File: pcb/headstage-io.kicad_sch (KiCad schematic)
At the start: 5 parts, among them J2 BTE-040-03-L-D-A, J3 BTE-040-03-L-D-A

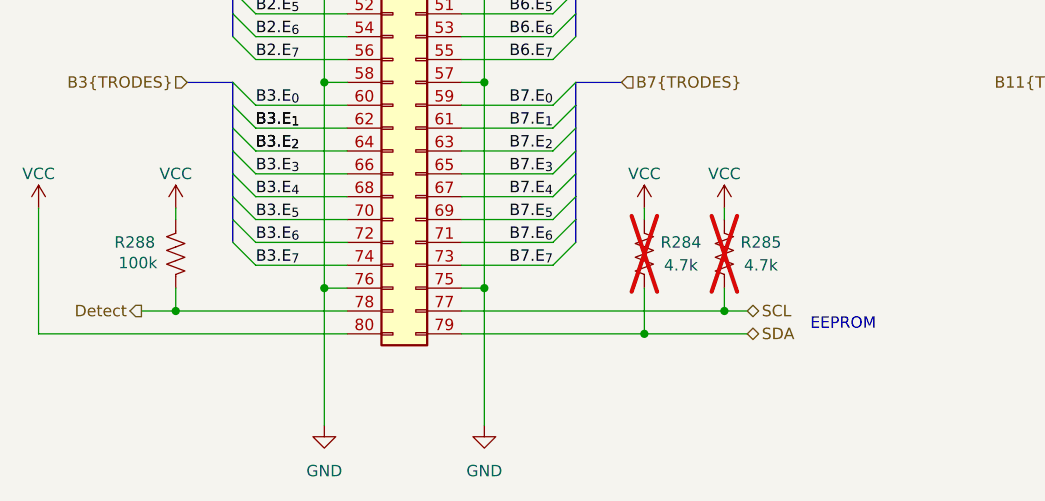
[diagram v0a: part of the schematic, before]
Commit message: Fix electrode coupling
- AC coupling follows attentuation to prevent high-pass filtering
- Remove redundant i2c pullups (can be enabled in MCU if really needed)
- Replace detect line with WP/Detect so that this device can be used to
  program module EEPROM by pulling the line down
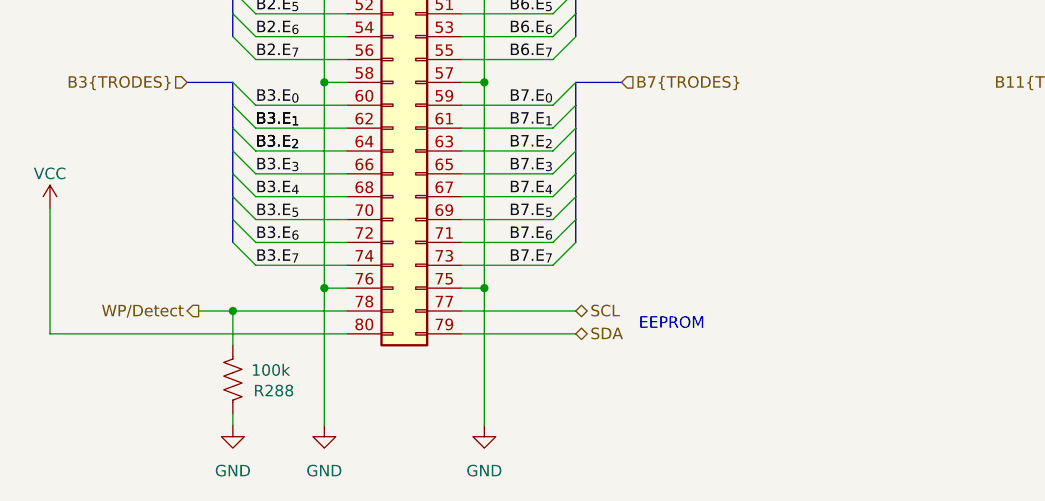
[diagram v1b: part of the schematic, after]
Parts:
- removed R284, R285: 4.7k, Resistor_SMD:R_0402_1005Metric, symbol Device:R_US
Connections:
- net GND: now also R288.1
- net VCC: no longer R288.1
- net Detect renamed WP/Detect
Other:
- moved on the sheet: R288

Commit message: Reduce test signal attenuation
- From -60 dbV to -54 dbV
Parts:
- R288: Tolerance (none) -> 0.1%
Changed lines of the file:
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@@
+			)
+		)
+		(property "Tolerance" "0.1%"
+			(at 68.58 148.59 0)
+			(effects
+				(font
+					(size 1.27 1.27)
+				)
+				(hide yes)
 			)
 		)
@@
 				)
 				(hide yes)
+			)
+		)
+		(property "Tolerance" ""
+			(at 194.31 92.71 0)
+			(effects
+				(font
+					(size 1.27 1.27)
+				)
 			)
 		)
@@
 			)
 		)
+		(property "Tolerance" ""
+			(at 88.9 92.71 0)
+			(effects
+				(font
+					(size 1.27 1.27)
+				)
+			)
+		)

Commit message: Added OEPS PN.
Co-Authored-By: David Palma <78764277+davidpalma666@users.noreply.github.com>
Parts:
- J2, J3: MPN (none) -> BTE-040-03-L-D-A; OEPSPN (none) -> OEPS070103
- R288: MPN (none) -> RG1005P-104-B-T5; OEPSPN (none) -> OEPS020175
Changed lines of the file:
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@@
+			)
+		)
+		(property "MPN" "RG1005P-104-B-T5"
+			(at 68.58 148.59 0)
+			(effects
+				(font
+					(size 1.27 1.27)
+				)
+				(hide yes)
+			)
+		)
+		(property "OEPSPN" "OEPS020175"
+			(at 68.58 148.59 0)
+			(effects
+				(font
+					(size 1.27 1.27)
+				)
+				(hide yes)
 			)
 		)
@@
 					(size 1.27 1.27)
 				)
+			)
+		)
+		(property "MPN" "BTE-040-03-L-D-A"
+			(at 194.31 92.71 0)
+			(effects
+				(font
+					(size 1.27 1.27)
+				)
+				(hide yes)
+			)
+		)
+		(property "OEPSPN" "OEPS070103"
+			(at 194.31 92.71 0)
+			(effects
+				(font
+					(size 1.27 1.27)
+				)
+				(hide yes)
 			)
 		)
@@
 			)
 		)
+		(property "MPN" "BTE-040-03-L-D-A"
+			(at 88.9 92.71 0)
+			(effects
+				(font
+					(size 1.27 1.27)
+				)
+				(hide yes)
+			)
+		)
+		(property "OEPSPN" "OEPS070103"
+			(at 88.9 92.71 0)
+			(effects
+				(font
+					(size 1.27 1.27)
+				)
+				(hide yes)
+			)
+		)

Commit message: Use 1.25V reference voltage for electrode test signal
- This prevents large AC component when channel switch occurs.
- Previously the attenuator reference and nomimal electrode signals were
  both ground. Since the test signal is centered arround 1.25V, there
  the test signal is effectively a 1.25V square wave + the indented
  signal. The square waves edges were readily passed through the AC
  coupling capacitor.
- Add LCSC numbers to all required components for assembly.
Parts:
- J2, J3: LCSC (none) -> C6135791
- R288: LCSC (none) -> C852472
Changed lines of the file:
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@@
+			)
+		)
+		(property "LCSC" "C852472"
+			(at 68.58 148.59 0)
+			(effects
+				(font
+					(size 1.27 1.27)
+				)
+				(hide yes)
 			)
 		)
@@
 		)
 		(property "OEPSPN" "OEPS070103"
+			(at 194.31 92.71 0)
+			(effects
+				(font
+					(size 1.27 1.27)
+				)
+				(hide yes)
+			)
+		)
+		(property "LCSC" "C6135791"
 			(at 194.31 92.71 0)
 			(effects
@@
 			(at 88.9 92.71 0)
 			(effects
+				(font
+					(size 1.27 1.27)
+				)
+				(hide yes)
+			)
+		)
+		(property "LCSC" "C6135791"
+			(at 88.9 92.71 0)
+			(effects

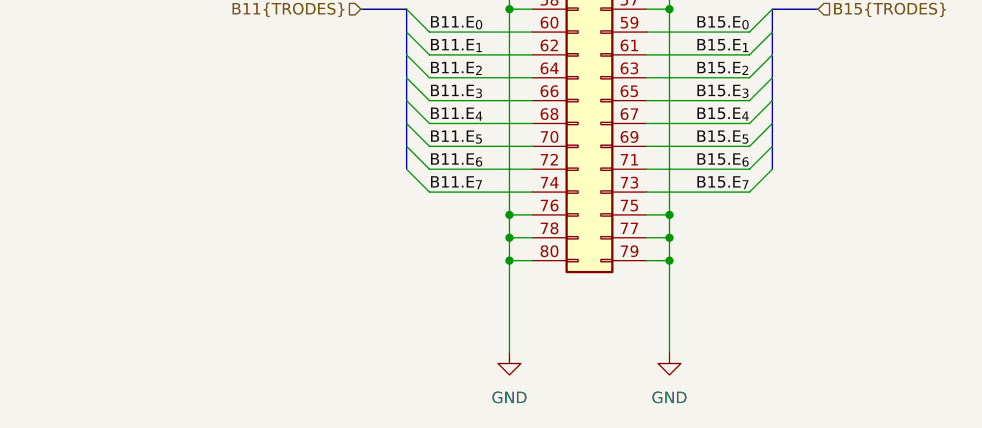
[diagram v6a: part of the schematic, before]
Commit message: Added dedicated TESTREF pin on headstage interface
- Also removed GND conenctions from 3 pins and marked as reserved
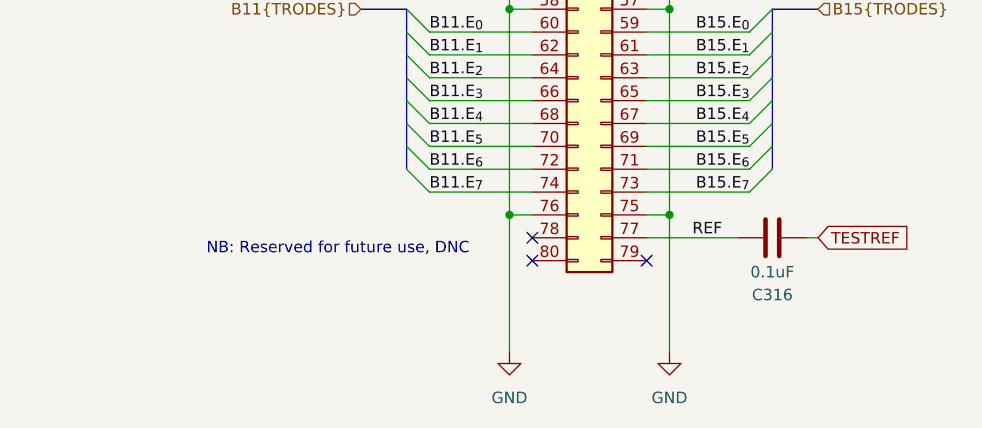
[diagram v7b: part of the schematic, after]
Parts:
- added C316: 0.1uF, Capacitor_SMD:C_0402_1005Metric, symbol Device:C
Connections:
- net GND: no longer J3.77 (Pin_77), J3.78 (Pin_78), J3.79 (Pin_79), J3.80 (Pin_80)
- new net REF: C316.2, J3.77 (Pin_77)
- new net TESTREF: C316.1
- no-connect marks 0 -> 3
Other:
- note added: "NB: Reserved for future use, DNC"
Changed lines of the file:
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@@
 		)
 	)
+	(text "NB: Reserved for future use, DNC"
+		(exclude_from_sim no)
+		(at 165.1 142.24 0)
+		(effects
+			(font
+				(size 1.27 1.27)
+			)
+		)
+	)
 	(junction
 		(at 184.15 69.85)
@@
 	)
 	(junction
-		(at 201.93 143.51)
-		(diameter 0)
-		(color 0 0 0 0)
-	)
-	(junction
 		(at 78.74 46.99)
 		(diameter 0)
@@
 	)
 	(junction
-		(at 184.15 143.51)
-		(diameter 0)
-		(color 0 0 0 0)
-	)
-	(junction
 		(at 184.15 138.43)
 		(diameter 0)
@@
 	)
 	(junction
-		(at 201.93 140.97)
-		(diameter 0)
-		(color 0 0 0 0)
-	)
-	(junction
 		(at 78.74 92.71)
 		(diameter 0)
@@
 	)
 	(junction
-		(at 184.15 140.97)
-		(diameter 0)
-		(color 0 0 0 0)
-	)
-	(junction
 		(at 96.52 115.57)
 		(diameter 0)
 		(color 0 0 0 0)
 	)
+	(no_connect
+		(at 186.69 140.97)
+	)
+	(no_connect
+		(at 186.69 143.51)
+	)
+	(no_connect
+		(at 199.39 143.51)
+	)
 	(bus_entry
 		(at 68.58 100.33)
@@
 	(wire
 		(pts
-			(xy 201.93 140.97) (xy 201.93 143.51)
+			(xy 201.93 138.43) (xy 201.93 153.67)
 		)
 		(stroke
@@
 		)
 	)
-	(wire
-		(pts
-			(xy 199.39 140.97) (xy 201.93 140.97)
-		)
-		(stroke
-			(width 0)
-			(type default)
-		)
-	)
 	(bus
 		(pts
@@
 	(wire
 		(pts
-			(xy 186.69 140.97) (xy 184.15 140.97)
-		)
-		(stroke
-			(width 0)
-			(type default)
-		)
-	)
-	(wire
-		(pts
 			(xy 78.74 138.43) (xy 78.74 153.67)
 		)
@@
 	(wire
 		(pts
-			(xy 184.15 140.97) (xy 184.15 143.51)
+			(xy 184.15 138.43) (xy 184.15 153.67)
 		)
 		(stroke
@@
 	(wire
 		(pts
-			(xy 199.39 143.51) (xy 201.93 143.51)
-		)
-		(stroke
-			(width 0)
-			(type default)
-		)
-	)
-	(wire
-		(pts
 			(xy 71.12 105.41) (xy 81.28 105.41)
 		)
@@
 	(wire
 		(pts
-			(xy 201.93 138.43) (xy 201.93 140.97)
-		)
-		(stroke
-			(width 0)
-			(type default)
-		)
-	)
-	(wire
-		(pts
 			(xy 199.39 133.35) (xy 210.82 133.35)
 		)
@@
 		)
 	)
-	(wire
-		(pts
-			(xy 184.15 143.51) (xy 186.69 143.51)
-		)
-		(stroke
-			(width 0)
-			(type default)
-		)
-	)
 	(bus
 		(pts
@@
 	(wire
 		(pts
-			(xy 184.15 138.43) (xy 184.15 140.97)
-		)
-		(stroke
-			(width 0)
-			(type default)
-		)
-	)
-	(wire
-		(pts
 			(xy 175.26 80.01) (xy 186.69 80.01)
 		)
@@
 	(wire
 		(pts
-			(xy 184.15 153.67) (xy 184.15 143.51)
+			(xy 199.39 140.97) (xy 209.55 140.97)
 		)
 		(stroke
@@
 	(wire
 		(pts
-			(xy 199.39 123.19) (xy 210.82 123.19)
+			(xy 217.17 140.97) (xy 218.44 140.97)
 		)
 		(stroke
@@
 		)
 	)
-	(bus
+	(wire
 		(pts
-			(xy 167.64 46.99) (xy 172.72 46.99)
+			(xy 199.39 123.19) (xy 210.82 123.19)
 		)
 		(stroke
@@
 	(bus
 		(pts
-			(xy 213.36 85.09) (xy 213.36 87.63)
+			(xy 167.64 46.99) (xy 172.72 46.99)
 		)
 		(stroke
@@
 		)
 	)
-	(wire
+	(bus
 		(pts
-			(xy 71.12 135.89) (xy 81.28 135.89)
+			(xy 213.36 85.09) (xy 213.36 87.63)
 		)
 		(stroke
@@
 	(wire
 		(pts
-			(xy 201.93 143.51) (xy 201.93 153.67)
+			(xy 71.12 135.89) (xy 81.28 135.89)
 		)
 		(stroke
@@
 		)
 	)
+	(label "REF"
+		(at 204.47 140.97 0)
+		(effects
+			(font
+				(size 1.27 1.27)
+			)
+			(justify left bottom)
+		)
+	)
 	(label "B8.E_{7}"
 		(at 175.26 67.31 0)
@@
 		)
 	)
+	(global_label "TESTREF"
+		(shape input)
+		(at 218.44 140.97 0)
+		(fields_autoplaced yes)
+		(effects
+			(font
+				(size 1.27 1.27)
+			)
+			(justify left)
+		)
+		(property "Intersheetrefs" "${INTERSHEET_REFS}"
+			(at 229.2265 140.97 0)
+			(effects
+				(font
+					(size 1.27 1.27)
+				)
+				(justify left)
+				(hide yes)
+			)
+		)
+	)
 	(hierarchical_label "B0{TRODES}"
 		(shape input)
@@
 					(unit 1)
 				)
+			)
+		)
+	)
+	(symbol
+		(lib_id "Device:C")
+		(at 213.36 140.97 270)
+		(unit 1)
+		(exclude_from_sim no)
+		(in_bom yes)
+		(on_board yes)
+		(dnp no)
+		(property "Reference" "C316"
+			(at 213.36 147.32 90)
+			(effects
+				(font
+					(size 1.27 1.27)
+				)
+			)
+		)
+		(property "Value" "0.1uF"
+			(at 213.36 144.78 90)
+			(effects
+				(font
+					(size 1.27 1.27)
+				)
+			)
+		)
+		(property "Footprint" "Capacitor_SMD:C_0402_1005Metric"
+			(at 209.55 141.9352 0)
+			(effects
+				(font
+					(size 1.27 1.27)
+				)
+				(hide yes)
+			)
+		)
+		(property "Datasheet" "~"
+			(at 213.36 140.97 0)
+			(effects
+				(font
+					(size 1.27 1.27)
+				)
+				(hide yes)
+			)
+		)
+		(property "Description" "Unpolarized capacitor"
+			(at 213.36 140.97 0)
+			(effects
+				(font
+					(size 1.27 1.27)
+				)
+				(hide yes)
+			)
+		)
+		(property "TempCo" "X7R"
+			(at 213.36 140.97 0)
+			(effects
+				(font
+					(size 1.27 1.27)
+				)
+				(hide yes)
+			)
+		)
+		(property "Voltage" "25V"
+			(at 213.36 140.97 0)
+			(effects
+				(font
+					(size 1.27 1.27)
+				)
+				(hide yes)
+			)
+		)
+		(property "Datasheet1" ""
+			(at 213.36 140.97 0)
+			(effects
+				(font
+					(size 1.27 1.27)
+				)
+				(hide yes)
+			)
+		)
+		(property "Part No." ""
+			(at 213.36 140.97 0)
+			(effects
+				(font
+					(size 1.27 1.27)
+				)
+				(hide yes)
+			)
+		)
+		(property "Tolerance" ""
+			(at 213.36 140.97 0)
+			(effects
+				(font
+					(size 1.27 1.27)
+				)
+			)
+		)
+		(property "MPN" "C1005X7R1E104K050BB"
+			(at 213.36 140.97 0)
+			(effects
+				(font
+					(size 1.27 1.27)
+				)
+				(hide yes)
+			)
+		)
+		(property "OEPSPN" "OEPS010050"
+			(at 213.36 140.97 0)
+			(effects
+				(font
+					(size 1.27 1.27)
+				)
+				(hide yes)
+			)
+		)
+		(property "LCSC" "C105883"
+			(at 213.36 140.97 90)
+			(effects
+				(font
+					(size 1.27 1.27)
+				)
+				(hide yes)
+			)
+		)
+		(pin "1"
+		)
+		(pin "2"
+		)
+		(instances
+			(project "ephys-test-board"
+				(path "/ffaa6ffd-73fa-4da3-9ff1-78fa7369281f/f2c6d928-7acb-4b4d-942a-bf07e4ec8d7a"
+					(reference "C316")
+					(unit 1)
+				)
